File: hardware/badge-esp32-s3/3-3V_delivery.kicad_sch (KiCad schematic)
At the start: 1 part, among them U2 AMS1117

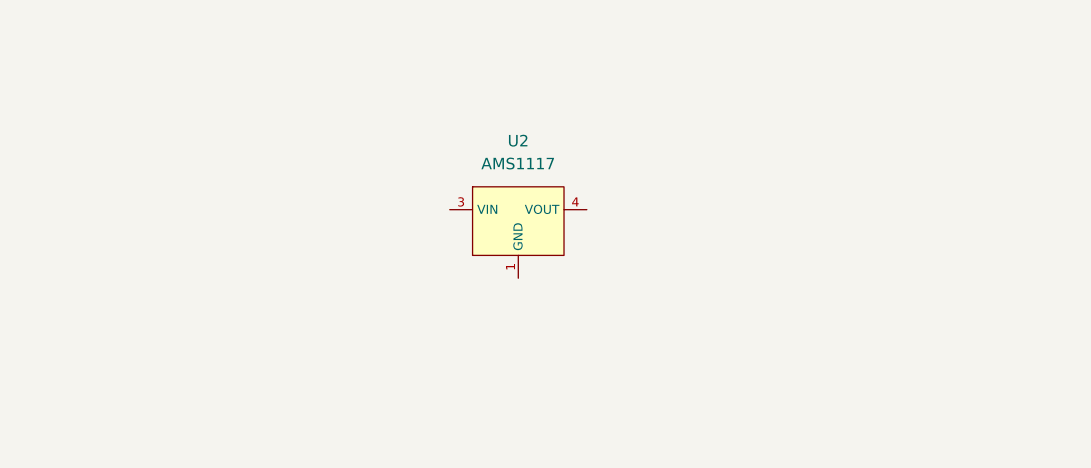
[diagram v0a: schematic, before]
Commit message: Finish linear regulator, start uart interface
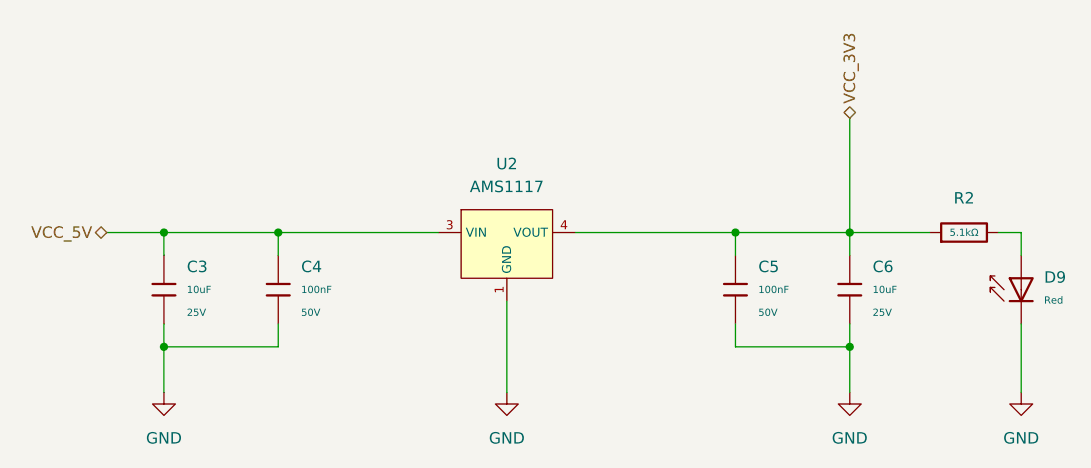
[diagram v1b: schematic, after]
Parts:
- added C3, C6: 10uF, PCM_JLCPCB:C_0603, symbol PCM_JLCPCB-Capacitors:0603,10uF,(2)
- added C4, C5: 100nF, PCM_JLCPCB:C_0603, symbol PCM_JLCPCB-Capacitors:0603,100nF
- added D9: Red, PCM_JLCPCB:D_0603, symbol PCM_JLCPCB-Diodes:LED,0603,Red
- added R2: 5.1kΩ, PCM_JLCPCB:R_0402, symbol PCM_JLCPCB-Resistors:0402,5.1kΩ
- U2: Stock 441791 -> 410193
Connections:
- net GND: now reaches U2.1 (GND)
- net GND: now also C3.2, C4.2, C5.2, C6.2, D9.1
- net VCC_3V3: now reaches U2.2 (VOUT), U2.4 (VOUT)
- net VCC_3V3: now also C5.1, C6.1, R2.1
- net VCC_5V: now reaches U2.3 (VIN)
- net VCC_5V: now also C3.1, C4.1
- new net: D9.2, R2.2
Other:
- moved on the sheet: U2

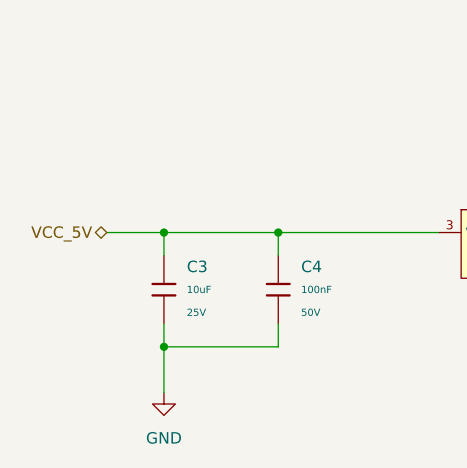
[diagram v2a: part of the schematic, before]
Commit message: Make progress on charger, switch out some diodes
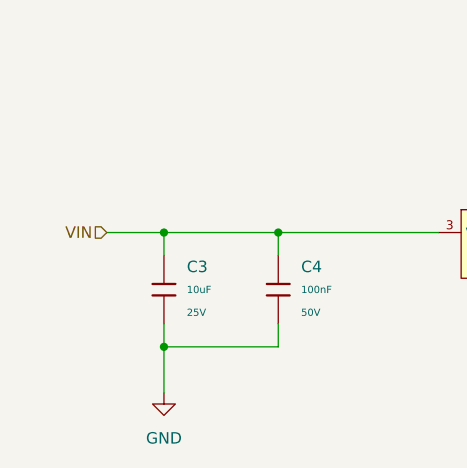
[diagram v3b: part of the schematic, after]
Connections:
- net VCC_5V renamed VIN
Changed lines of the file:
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@@
 		)
 	)
-	(hierarchical_label "VCC_5V"
-		(shape bidirectional)
+	(hierarchical_label "VIN"
+		(shape input)
 		(at 101.6 63.5 180)
 		(effects

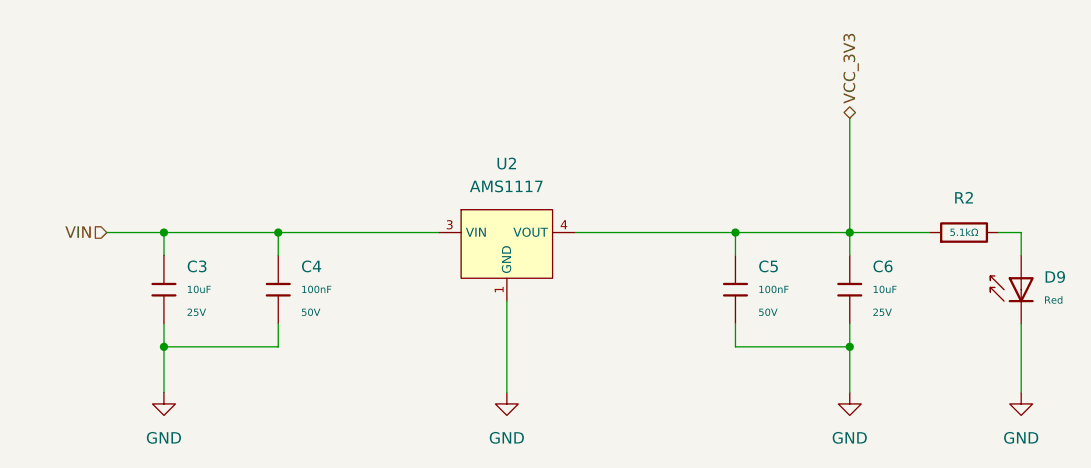
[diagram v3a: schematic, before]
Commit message: Finish charging circuit Switched out schottky diodes Better linear regulator
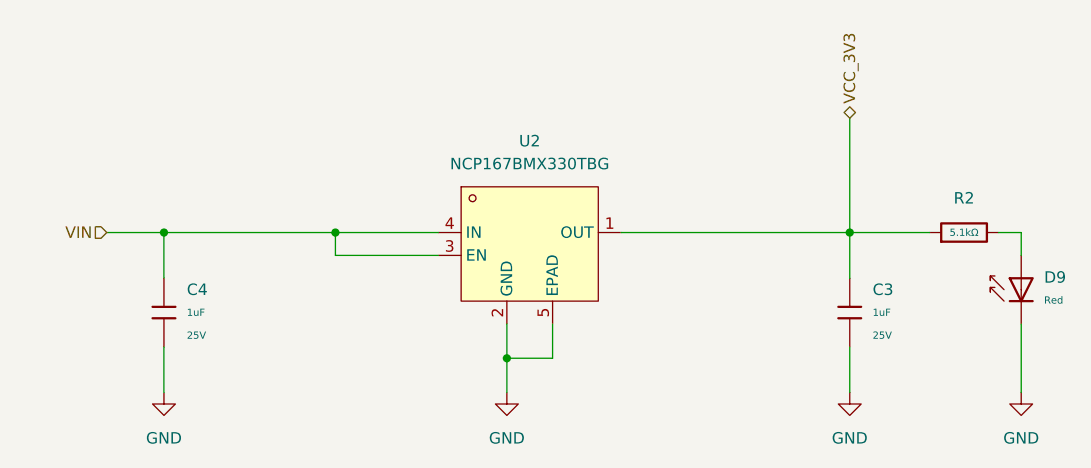
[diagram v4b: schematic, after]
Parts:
- removed C3, C6: 10uF, PCM_JLCPCB:C_0603, symbol PCM_JLCPCB-Capacitors:0603,10uF,(2)
- removed C4, C5: 100nF, PCM_JLCPCB:C_0603, symbol PCM_JLCPCB-Capacitors:0603,100nF
- removed U2: AMS1117, PCM_JLCPCB:SOT-223-3_L6.5-W3.4-P2.30-LS7.0-BR, symbol PCM_JLCPCB-Power:LDO, 3.3V, 1A
- added C3, C4: 1uF, PCM_JLCPCB:C_0402, symbol PCM_JLCPCB-Capacitors:0402,1uF
- added U2: NCP167BMX330TBG, lcsc-lib:XDFN-4_L1.0-W1.0-P0.65-BL-EP, symbol lcsc-lib:NCP167BMX330TBG
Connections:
- net GND: now also C3.2, C4.2, U2.2 (GND), U2.5 (EPAD)
- net VCC_3V3: now also C3.1, U2.1 (OUT)
- net VIN: now also C4.1, U2.3 (EN), U2.4 (IN)
